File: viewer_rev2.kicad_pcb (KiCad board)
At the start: 2 copper layers, 128 x 108 mm, 211 parts, among them J2 USB_C_Receptacle_USB2.0_16P, Q1 ZXMN4A06GTA, SW1 SW_SPDT, U1 TLC555xD

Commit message: Add DigiKey and Mouser PNs. Update manf outputs
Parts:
- R10, R100, R101, R11, R12, R13, R14, R15, R16, R17, R18, R19, R20, R21, R22, R23, R24, R25, R26, R27, R28, R29, R30, R31, R32, R33, R34, R35, R36, R37, R38, R39, R40, R41, R42, R43, R44, R45, R46, R47, R48, R49, R50, R51, R52, R53, R54, R55, R56, R57, R58, R59, R6, R60, R61, R62, R63, R64, R65, R66, R67, R68, R69, R7, R70, R71, R72, R73, R74, R75, R76, R77, R78, R79, R8, R80, R81, R82, R83, R84, R85, R86, R87, R88, R89, R9, R90, R91, R92, R93, R94, R95, R96, R97, R98, R99: value 91 -> 100

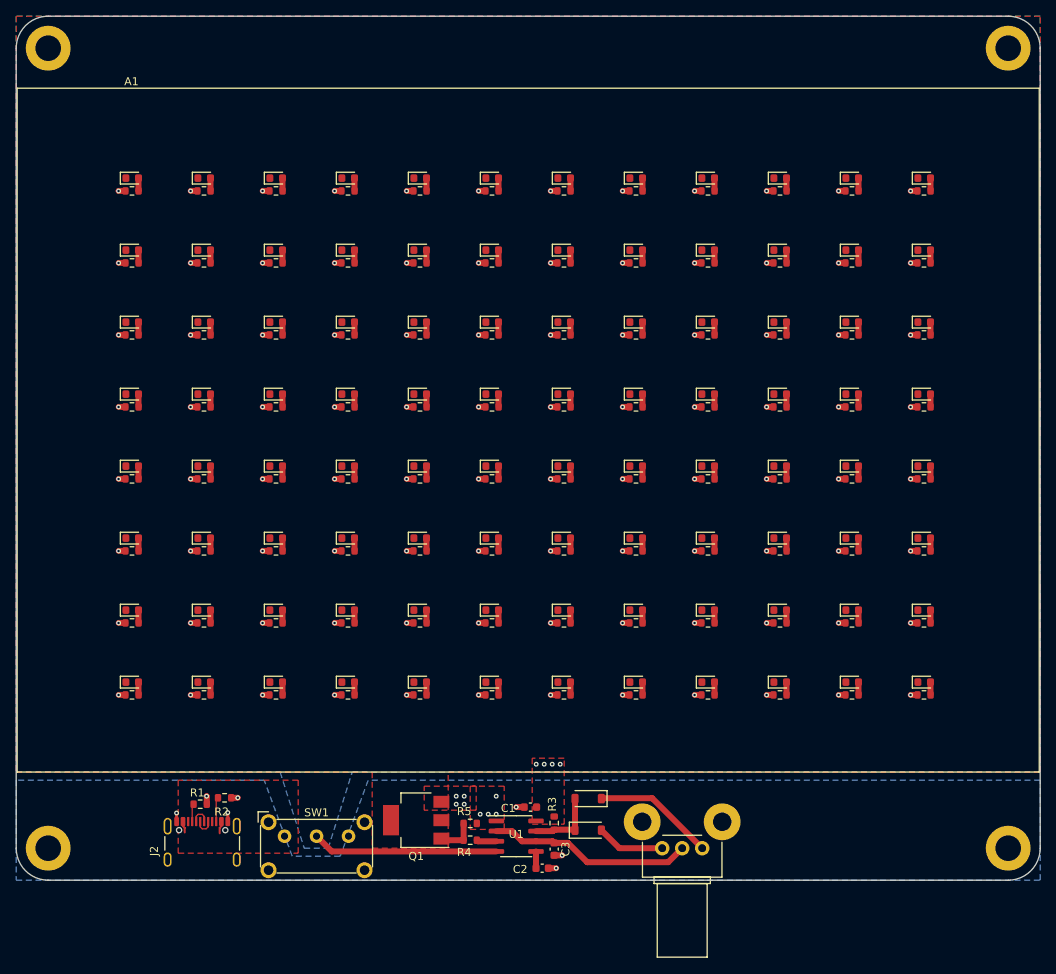
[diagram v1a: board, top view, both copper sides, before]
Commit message: part change to higher current switch. Export manf for new PCB and new BOM.
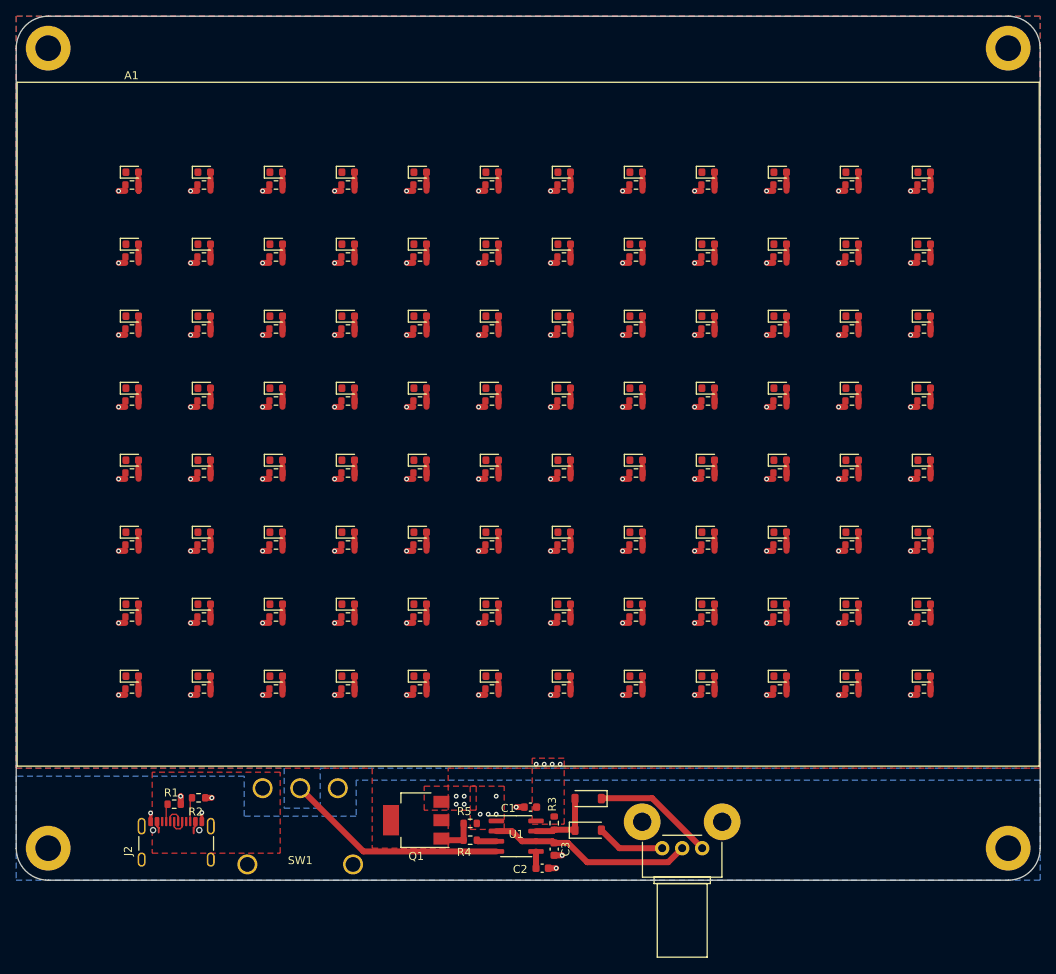
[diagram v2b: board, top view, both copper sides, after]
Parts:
- SW1: footprint Button_Switch_THT:SW_E-Switch_EG1224_SPDT_Angled -> Switch:1101MxSxAxx
- moved SW1 4.03 mm to (139.0, 135.0)
- moved R2 3.25 mm to (126.3, 126.7)
- moved J2 3.25 mm to (123.5, 133.3)
- moved R1 3.25 mm to (123.2, 127.5)
- moved R100 0.74 mm to (208.0, 113.1)
- moved R101 0.74 mm to (217.0, 113.1)
- moved R30 0.74 mm to (118.0, 68.1)
- moved R31 0.74 mm to (127.0, 68.1)
- moved R32 0.74 mm to (136.0, 68.1)
- moved R33 0.74 mm to (145.0, 68.1)
- moved R34 0.74 mm to (154.0, 68.1)
- moved R35 0.74 mm to (163.0, 68.1)
- moved R36 0.74 mm to (172.0, 68.1)
- moved R37 0.74 mm to (181.0, 68.1)
- moved R38 0.74 mm to (190.0, 68.1)
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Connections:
- J2 pad A4: Net-(SW1-A) -> Net-(SW1-C)
- J2 pad A9: Net-(SW1-A) -> Net-(SW1-C)
- J2 pad B4: Net-(SW1-A) -> Net-(SW1-C)
- J2 pad B9: Net-(SW1-A) -> Net-(SW1-C)
- SW1 pad 1: Net-(SW1-A) -> unconnected-(SW1-A-Pad1)
- SW1 pad 3: unconnected-(SW1-C-Pad3) -> Net-(SW1-C)
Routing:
- net VCC: track 103.9 -> 108.5 mm
- net Net-(SW1-C): track 0.00 -> 3.01 mm
- net Net-(SW1-A): track 3.01 -> 0.00 mm
- added copper zone on F.Cu, net Net-(SW1-C)
- removed copper zone on F.Cu, net Net-(SW1-A)
